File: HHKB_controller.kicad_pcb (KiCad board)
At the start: 2 copper layers, 141.5 x 36 mm, 94 parts, among them CN1 CONN_15, CN2 CONN_13, J1 USB_MINI_MICRO_B, P15 CONN_3X2, P16 CONN_2, P26 CONN_1, P27 CONN_1, P28 CONN_1, P29 CONN_1, P30 CONN_1, Q1 MOSFET_N, Q2 MOSFET_N, SW1 SW_PUSH, SW2 DPDT, U1 ATMEGA32U4, U2 TAR5SB33, U3 HT7750A, U4 LTC4054, U5 WT12_BLUEGIGA, X1 8/16MHz

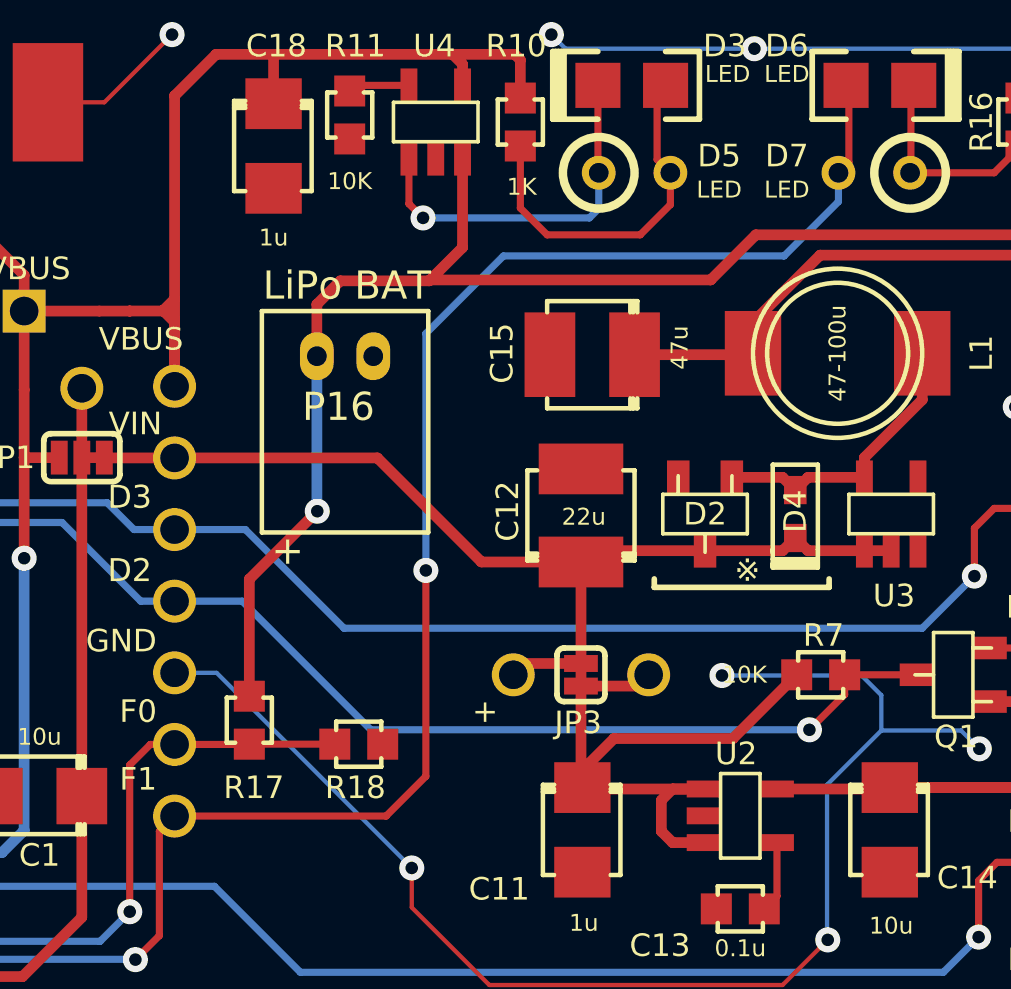
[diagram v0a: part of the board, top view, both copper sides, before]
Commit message: Replace Lipo connector with SMT component
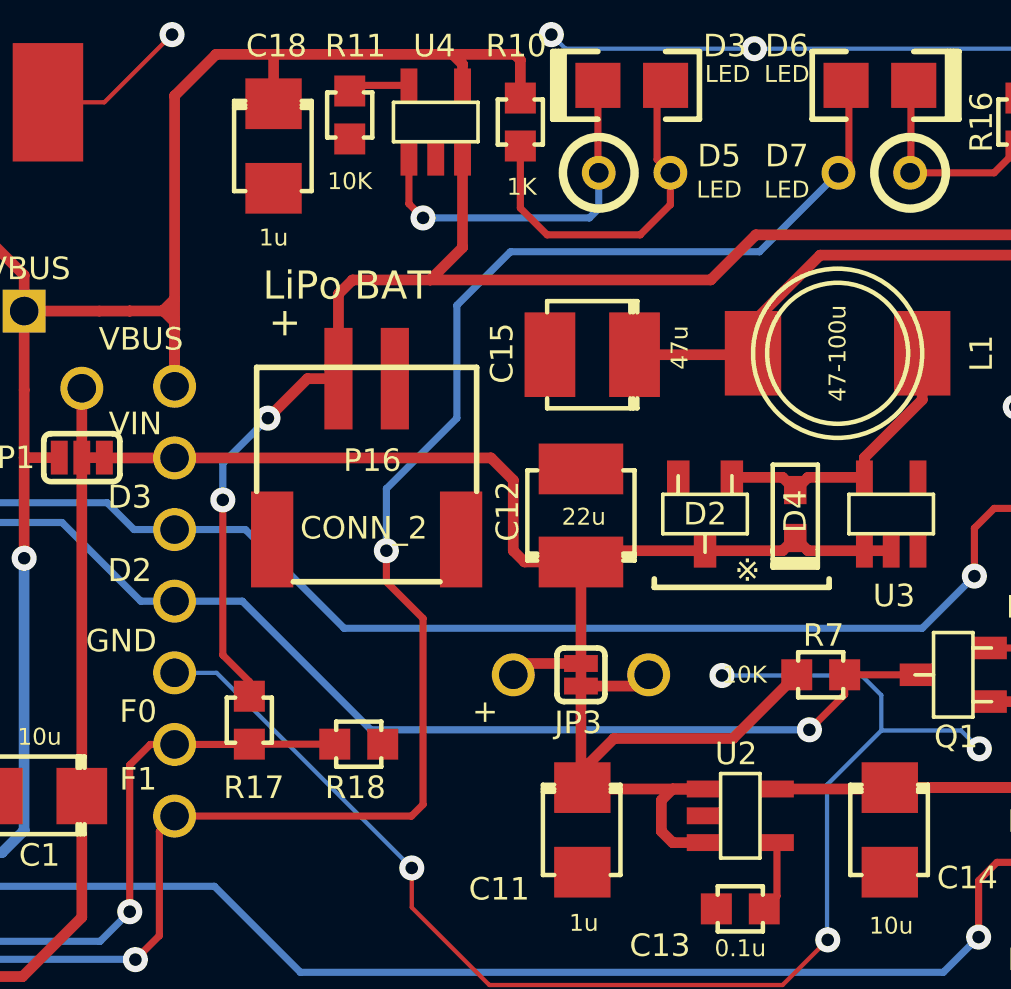
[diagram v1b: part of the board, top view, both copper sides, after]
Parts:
- P16: footprint JST_PH2_TH -> JST_PH2_SMT
- moved P16 0.83 mm to (157.9, 94.3), turned to 0 degrees
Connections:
- P16 pad 1: GND -> N-0000047
- P16 pad 2: N-0000047 -> GND
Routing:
- net VIN: track 263.5 -> 265.0 mm
- net N-0000047: track 65.8 -> 67.0 mm, vias 1 -> 2
- net BT_INDICATOR: track 76.0 -> 77.0 mm

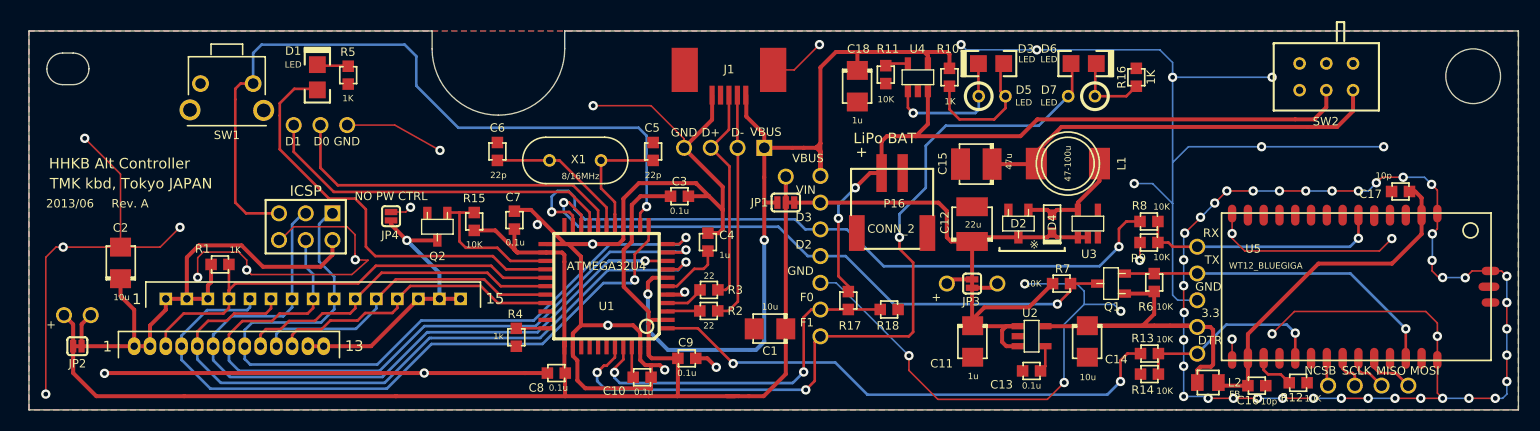
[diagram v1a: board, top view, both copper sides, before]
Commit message: Fix USB controller part
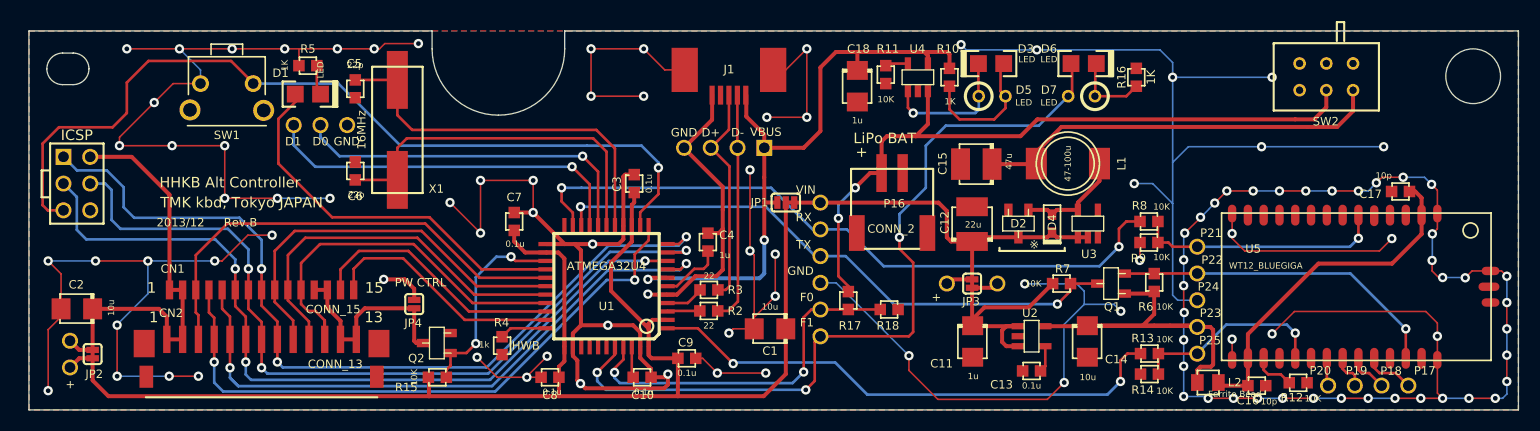
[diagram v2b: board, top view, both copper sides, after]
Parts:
- removed P30: CONN_1, PIN_1
- removed R1: 1K, R_1608
- removed the VBUS at (152.1, 94.6)
- CN1: footprint HHKB_PRO_PH15 -> HHKB_JP_HRS_DF14_15P
- CN2: footprint HHKB_PRO2_ZH13_TH -> HHKB_PRO2_ZH13
- L2: value FB -> Ferrite Bead
- P15: value CONN_3X2 -> ICSP; footprint pin_array_3x2 -> AVR_ICSP_3x2
- SW2: value DPDT -> SPST
- X1: value 8/16MHz -> 16MHz; footprint XTAL_HC_49_TH -> HC-49_SMT
- moved C5 28.9 mm to (107.9, 86.3), turned to 270 degrees
- moved P15 22.1 mm to (81.5, 95.3), turned to 270 degrees
- moved X1 17.1 mm to (111.9, 90.2), turned to 270 degrees
- moved R15 15.2 mm to (115.7, 113.7), turned to 0 degrees
- moved C6 13.6 mm to (107.9, 94.1)
- moved Q2 11.1 mm to (115.7, 110.5), turned to 90 degrees
- moved JP4 8.63 mm to (113.5, 106.8)
- moved C2 6.02 mm to (81.5, 107.2), turned to 180 degrees
- moved CN2 5.94 mm to (90.0, 110.1), turned to 0 degrees
- moved P27 5.00 mm to (80.8, 112.8), turned to 90 degrees
- moved C3 4.46 mm to (134.4, 95.3), turned to 90 degrees
- moved CN1 3.94 mm to (107.8, 105.4), turned to 180 degrees
- moved R5 3.93 mm to (103.4, 84.1), turned to 180 degrees
- moved P26 3.13 mm to (80.8, 110.2), turned to 90 degrees
- moved D1 1.84 mm to (103.4, 86.8), turned to 0 degrees
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- renumbered MOSI to P17, MISO to P18, SCLK to P19, NCSB to P20, RX to P21, TX to P22, 3.3 to P23, GND to P24, DTR to P25, D3 to RX, D2 to TX
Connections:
- CN1 pad 10: /PB4 -> /PB5
- CN1 pad 11: /PB5 -> /PB6
- CN1 pad 12: /PB6 -> /HHKB_GND
- CN1 pad 14: /HHKB_GND -> /PC6
- CN1 pad 15: /HHKB_GND -> /PC7
- CN1 pad 3: VIN -> /PD7
- CN1 pad 4: /PD7 -> /PB7
- CN1 pad 5: /PB7 -> /PB0
- CN1 pad 6: /PB0 -> /PB1
- CN1 pad 7: /PB1 -> /PB2
- CN1 pad 8: /PB2 -> /PB3
- CN1 pad 9: /PB3 -> /PB4
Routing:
- net GND: track 506.3 -> 584.1 mm, vias 75 -> 108
- net /PC6: track 0.00 -> 24.6 mm
- net N-0000041: track 12.9 -> 36.7 mm
- net /PC7: track 0.00 -> 23.1 mm
- net VIN: track 265.0 -> 243.0 mm
- net N-0000040: track 14.0 -> 34.9 mm
- net VBUS: track 80.2 -> 61.4 mm
- net /~RESET: track 72.0 -> 82.3 mm
- net /PB3: track 71.7 -> 81.9 mm, vias 1 -> 3
- net /PB2: track 68.8 -> 78.4 mm, vias 1 -> 3
- net /HHKB_GND: track 28.6 -> 20.0 mm, vias 1 -> 0
- net /PB6: track 28.3 -> 36.8 mm
- net /PB5: track 30.1 -> 36.3 mm
- net /PB4: track 31.8 -> 37.9 mm
- net /PB7: track 64.9 -> 59.4 mm, vias 1 -> 2
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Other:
- board text added: "2013/12"
- board text added: "HWB"
- board text added: "PW CTRL"
- board text added: "Rev.B"
- board text removed: "2013/06"
- board text removed: "NO PW CTRL"
- board text removed: "Rev. A"

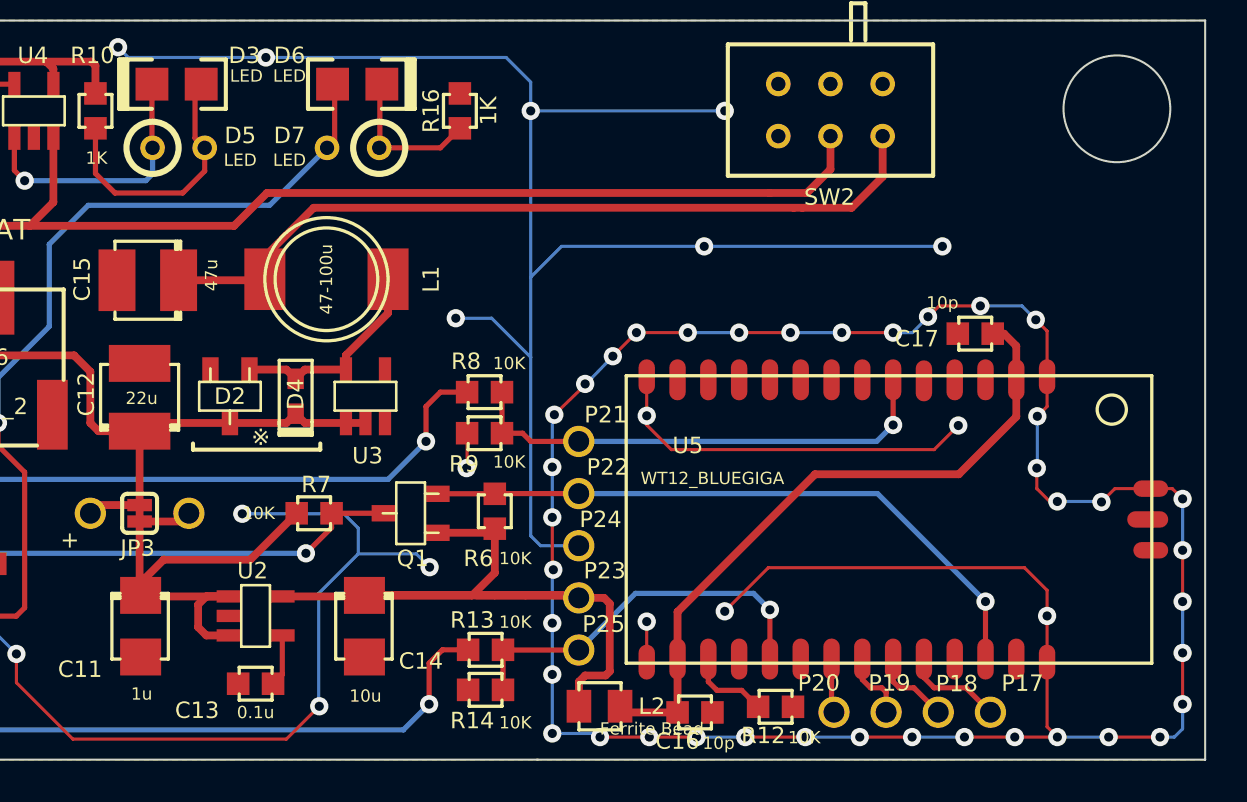
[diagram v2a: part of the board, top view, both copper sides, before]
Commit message: Add Power Source Selector
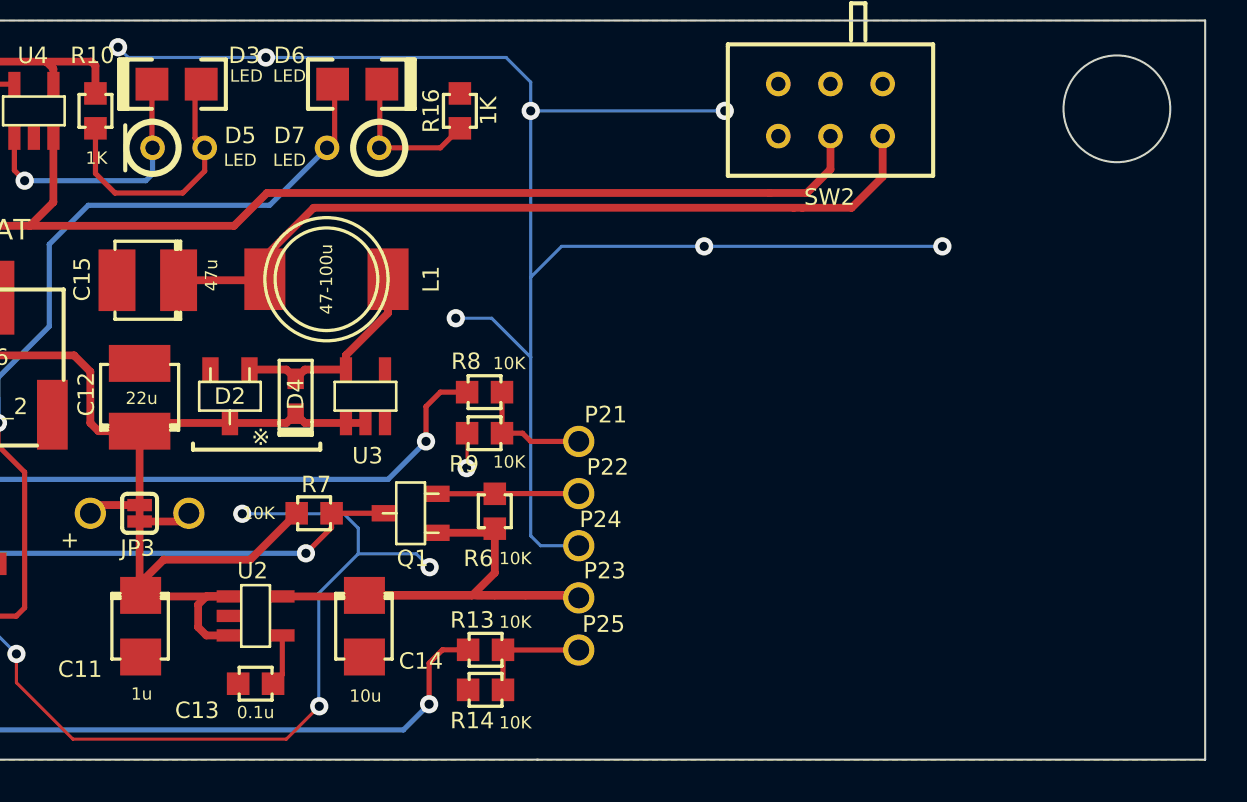
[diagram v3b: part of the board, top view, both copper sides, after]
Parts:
- removed C16, C17: 10p, C_1608
- removed L2: Ferrite Bead, R_2012
- removed P17, P18, P19, P20: CONN_1, PIN_1
- removed R12: 10K, R_1608
- removed U5: WT12_BLUEGIGA, WT12_bluegiga
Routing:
- net GND: track 584.1 -> 438.5 mm, vias 108 -> 64
- net N-0000043: track 33.1 -> 0.00 mm
- net /bluetooth/TX_33: track 31.7 -> 6.89 mm, vias 1 -> 0
- net /bluetooth/RX_33: track 23.7 -> 5.91 mm, vias 1 -> 0
- net /bluetooth/DTR_33: track 18.8 -> 5.64 mm, vias 1 -> 0
- net +3.3V: track 39.2 -> 31.4 mm
- net /bluetooth/MOSI: track 4.84 -> 0.00 mm
- net /bluetooth/SCLK: track 4.12 -> 0.00 mm
- net N-0000050: track 4.03 -> 0.00 mm
- net /bluetooth/MISO: track 3.92 -> 0.00 mm
- net /bluetooth/NCSB: track 2.64 -> 0.00 mm
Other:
- board text removed: "Bluegiga WT12 Breakout"
- board text removed: "TMK kbd"
